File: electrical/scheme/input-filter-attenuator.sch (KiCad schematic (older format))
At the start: 18 parts

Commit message: a.
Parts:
- removed C? (x2): 100n, symbol C
- removed R? (x2): 16 5%, symbol R
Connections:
- wire segments 47 -> 37
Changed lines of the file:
@@
 LIBS:adg5204
 LIBS:ad8620
+LIBS:ad5543
+LIBS:bat54s
 LIBS:digitizer-cache
 EELAYER 25 0
@@
 $Descr A4 11693 8268
 encoding utf-8
-Sheet 2 2
+Sheet 5 7
 Title ""
 Date ""
@@
 U 1 1 55A8C542
 P 5250 3850
+AR Path="/55A8BFF5/55A8C542" Ref="U?"  Part="1"
+AR Path="/55AAF91E/55A8C542" Ref="U?"  Part="1"
+AR Path="/55AAFE8D/55A8C542" Ref="U?"  Part="1"
+AR Path="/55AAFE9C/55A8C542" Ref="U?"  Part="1"
 F 0 "U?" H 5600 3650 60  0000 C CNN
 F 1 "AD8620" H 5600 4050 60  0000 C CNN
@@
 U 2 1 55A8C549
 P 8350 4050
+AR Path="/55A8BFF5/55A8C549" Ref="U?"  Part="2"
+AR Path="/55AAF91E/55A8C549" Ref="U?"  Part="2"
+AR Path="/55AAFE8D/55A8C549" Ref="U?"  Part="2"
+AR Path="/55AAFE9C/55A8C549" Ref="U?"  Part="2"
 F 0 "U?" H 8700 3850 60  0000 C CNN
 F 1 "AD8620" H 8700 4250 60  0000 C CNN
@@
 U 1 1 55A8C74B
 P 5250 2800
+AR Path="/55A8BFF5/55A8C74B" Ref="R?"  Part="1"
+AR Path="/55AAF91E/55A8C74B" Ref="R?"  Part="1"
+AR Path="/55AAFE8D/55A8C74B" Ref="R?"  Part="1"
+AR Path="/55AAFE9C/55A8C74B" Ref="R?"  Part="1"
 F 0 "R?" V 5330 2800 50  0000 C CNN
 F 1 "16 5%" V 5250 2800 50  0000 C CNN
@@
 U 1 1 55A8C77D
 P 5000 3050
+AR Path="/55A8BFF5/55A8C77D" Ref="C?"  Part="1"
+AR Path="/55AAF91E/55A8C77D" Ref="C?"  Part="1"
+AR Path="/55AAFE8D/55A8C77D" Ref="C?"  Part="1"
+AR Path="/55AAFE9C/55A8C77D" Ref="C?"  Part="1"
 F 0 "C?" H 5025 3150 50  0000 L CNN
 F 1 "100n" H 5025 2950 50  0000 L CNN
@@
 U 1 1 55A8C85F
 P 4650 3150
+AR Path="/55A8BFF5/55A8C85F" Ref="#PWR?"  Part="1"
+AR Path="/55AAF91E/55A8C85F" Ref="#PWR?"  Part="1"
+AR Path="/55AAFE8D/55A8C85F" Ref="#PWR?"  Part="1"
+AR Path="/55AAFE9C/55A8C85F" Ref="#PWR?"  Part="1"
 F 0 "#PWR?" H 4650 2900 50  0001 C CNN
 F 1 "GNDA" H 4650 3000 50  0000 C CNN
@@
 U 1 1 55A8C8A7
 P 5250 4800
+AR Path="/55A8BFF5/55A8C8A7" Ref="R?"  Part="1"
+AR Path="/55AAF91E/55A8C8A7" Ref="R?"  Part="1"
+AR Path="/55AAFE8D/55A8C8A7" Ref="R?"  Part="1"
+AR Path="/55AAFE9C/55A8C8A7" Ref="R?"  Part="1"
 F 0 "R?" V 5330 4800 50  0000 C CNN
 F 1 "16 5%" V 5250 4800 50  0000 C CNN
@@
 U 1 1 55A8CC9D
 P 5000 4550
+AR Path="/55A8BFF5/55A8CC9D" Ref="C?"  Part="1"
+AR Path="/55AAF91E/55A8CC9D" Ref="C?"  Part="1"
+AR Path="/55AAFE8D/55A8CC9D" Ref="C?"  Part="1"
+AR Path="/55AAFE9C/55A8CC9D" Ref="C?"  Part="1"
 F 0 "C?" H 5025 4650 50  0000 L CNN
 F 1 "100n" H 5025 4450 50  0000 L CNN
@@
 U 1 1 55A8CCA5
 P 4650 4650
+AR Path="/55A8BFF5/55A8CCA5" Ref="#PWR?"  Part="1"
+AR Path="/55AAF91E/55A8CCA5" Ref="#PWR?"  Part="1"
+AR Path="/55AAFE8D/55A8CCA5" Ref="#PWR?"  Part="1"
+AR Path="/55AAFE9C/55A8CCA5" Ref="#PWR?"  Part="1"
 F 0 "#PWR?" H 4650 4400 50  0001 C CNN
 F 1 "GNDA" H 4650 4500 50  0000 C CNN
@@
 $Comp
 L R R?
-U 1 1 55A8CE4E
-P 8350 3000
-F 0 "R?" V 8430 3000 50  0000 C CNN
-F 1 "16 5%" V 8350 3000 50  0000 C CNN
-F 2 "" V 8280 3000 30  0000 C CNN
-F 3 "" H 8350 3000 30  0000 C CNN
-	1    8350 3000
-	1    0    0    -1
-$EndComp
-$Comp
-L C C?
-U 1 1 55A8CE54
-P 8100 3250
-F 0 "C?" H 8125 3350 50  0000 L CNN
-F 1 "100n" H 8125 3150 50  0000 L CNN
-F 2 "" H 8138 3100 30  0000 C CNN
-F 3 "" H 8100 3250 60  0000 C CNN
-	1    8100 3250
-	0    1    1    0
-$EndComp
-Wire Wire Line
-	8350 3150 8350 3650
-Wire Wire Line
-	8250 3250 8350 3250
-Connection ~ 8350 3250
-Wire Wire Line
-	7950 3250 7750 3250
-Wire Wire Line
-	7750 3250 7750 3350
-$Comp
-L GNDA #PWR?
-U 1 1 55A8CE5F
-P 7750 3350
-F 0 "#PWR?" H 7750 3100 50  0001 C CNN
-F 1 "GNDA" H 7750 3200 50  0000 C CNN
-F 2 "" H 7750 3350 60  0000 C CNN
-F 3 "" H 7750 3350 60  0000 C CNN
-	1    7750 3350
-	1    0    0    -1
-$EndComp
-Wire Wire Line
-	8350 2850 8350 2500
-Text Label 8350 2650 1    60   ~ 0
-v+
-Wire Wire Line
-	8350 4450 8350 4850
-$Comp
-L R R?
-U 1 1 55A8CEC6
-P 8350 5000
-F 0 "R?" V 8430 5000 50  0000 C CNN
-F 1 "16 5%" V 8350 5000 50  0000 C CNN
-F 2 "" V 8280 5000 30  0000 C CNN
-F 3 "" H 8350 5000 30  0000 C CNN
-	1    8350 5000
-	1    0    0    -1
-$EndComp
-Wire Wire Line
-	8350 5150 8350 5450
-Text Label 8350 5400 1    60   ~ 0
-v-
-$Comp
-L C C?
-U 1 1 55A8CECE
-P 8100 4750
-F 0 "C?" H 8125 4850 50  0000 L CNN
-F 1 "100n" H 8125 4650 50  0000 L CNN
-F 2 "" H 8138 4600 30  0000 C CNN
-F 3 "" H 8100 4750 60  0000 C CNN
-	1    8100 4750
-	0    1    1    0
-$EndComp
-Wire Wire Line
-	7950 4750 7750 4750
-Wire Wire Line
-	7750 4750 7750 4850
-$Comp
-L GNDA #PWR?
-U 1 1 55A8CED6
-P 7750 4850
-F 0 "#PWR?" H 7750 4600 50  0001 C CNN
-F 1 "GNDA" H 7750 4700 50  0000 C CNN
-F 2 "" H 7750 4850 60  0000 C CNN
-F 3 "" H 7750 4850 60  0000 C CNN
-	1    7750 4850
-	1    0    0    -1
-$EndComp
-Wire Wire Line
-	8250 4750 8350 4750
-Connection ~ 8350 4750
-$Comp
-L R R?
 U 1 1 55A8D6B2
 P 3100 3650
+AR Path="/55A8BFF5/55A8D6B2" Ref="R?"  Part="1"
+AR Path="/55AAF91E/55A8D6B2" Ref="R?"  Part="1"
+AR Path="/55AAFE8D/55A8D6B2" Ref="R?"  Part="1"
+AR Path="/55AAFE9C/55A8D6B2" Ref="R?"  Part="1"
 F 0 "R?" V 3180 3650 50  0000 C CNN
 F 1 "806 1%" V 3100 3650 50  0000 C CNN
@@
 U 1 1 55A8D707
 P 3600 3650
+AR Path="/55A8BFF5/55A8D707" Ref="R?"  Part="1"
+AR Path="/55AAF91E/55A8D707" Ref="R?"  Part="1"
+AR Path="/55AAFE8D/55A8D707" Ref="R?"  Part="1"
+AR Path="/55AAFE9C/55A8D707" Ref="R?"  Part="1"
 F 0 "R?" V 3680 3650 50  0000 C CNN
 F 1 "1k91 1%" V 3600 3650 50  0000 C CNN
@@
 U 1 1 55A8D733
 P 3850 3900
+AR Path="/55A8BFF5/55A8D733" Ref="C?"  Part="1"
+AR Path="/55AAF91E/55A8D733" Ref="C?"  Part="1"
+AR Path="/55AAFE8D/55A8D733" Ref="C?"  Part="1"
+AR Path="/55AAFE9C/55A8D733" Ref="C?"  Part="1"
 F 0 "C?" H 3875 4000 50  0000 L CNN
 F 1 "22n" H 3875 3800 50  0000 L CNN
@@
 U 1 1 55A8D76D
 P 3350 3350
+AR Path="/55A8BFF5/55A8D76D" Ref="C?"  Part="1"
+AR Path="/55AAF91E/55A8D76D" Ref="C?"  Part="1"
+AR Path="/55AAFE8D/55A8D76D" Ref="C?"  Part="1"
+AR Path="/55AAFE9C/55A8D76D" Ref="C?"  Part="1"
 F 0 "C?" H 3375 3450 50  0000 L CNN
 F 1 "3u3" H 3375 3250 50  0000 L CNN
@@
 U 1 1 55A8D8D4
 P 6200 3850
+AR Path="/55A8BFF5/55A8D8D4" Ref="R?"  Part="1"
+AR Path="/55AAF91E/55A8D8D4" Ref="R?"  Part="1"
+AR Path="/55AAFE8D/55A8D8D4" Ref="R?"  Part="1"
+AR Path="/55AAFE9C/55A8D8D4" Ref="R?"  Part="1"
 F 0 "R?" V 6280 3850 50  0000 C CNN
 F 1 "9k31 1%" V 6200 3850 50  0000 C CNN
@@
 U 1 1 55A8DA7D
 P 6700 3850
+AR Path="/55A8BFF5/55A8DA7D" Ref="R?"  Part="1"
+AR Path="/55AAF91E/55A8DA7D" Ref="R?"  Part="1"
+AR Path="/55AAFE8D/55A8DA7D" Ref="R?"  Part="1"
+AR Path="/55AAFE9C/55A8DA7D" Ref="R?"  Part="1"
 F 0 "R?" V 6780 3850 50  0000 C CNN
 F 1 "21k 1%" V 6700 3850 50  0000 C CNN
@@
 U 1 1 55A8DD2D
 P 6450 3600
+AR Path="/55A8BFF5/55A8DD2D" Ref="C?"  Part="1"
+AR Path="/55AAF91E/55A8DD2D" Ref="C?"  Part="1"
+AR Path="/55AAFE8D/55A8DD2D" Ref="C?"  Part="1"
+AR Path="/55AAFE9C/55A8DD2D" Ref="C?"  Part="1"
 F 0 "C?" H 6475 3700 50  0000 L CNN
 F 1 "120n" H 6475 3500 50  0000 L CNN
@@
 U 1 1 55A8DF47
 P 7050 4200
+AR Path="/55A8BFF5/55A8DF47" Ref="C?"  Part="1"
+AR Path="/55AAF91E/55A8DF47" Ref="C?"  Part="1"
+AR Path="/55AAFE8D/55A8DF47" Ref="C?"  Part="1"
+AR Path="/55AAFE9C/55A8DF47" Ref="C?"  Part="1"
 F 0 "C?" H 7075 4300 50  0000 L CNN
 F 1 "22u" H 7075 4100 50  0000 L CNN
@@
 Wire Wire Line
 	8900 4050 9700 4050
-Wire Wire Line
-	9100 1950 9100 5750
-Wire Wire Line
-	9100 1950 6450 1950
-Wire Wire Line
-	6450 1950 6450 3450
 Connection ~ 9100 4050
 $Comp
@@
 U 1 1 55A8F5C0
 P 7050 4550
+AR Path="/55A8BFF5/55A8F5C0" Ref="#PWR?"  Part="1"
+AR Path="/55AAF91E/55A8F5C0" Ref="#PWR?"  Part="1"
+AR Path="/55AAFE8D/55A8F5C0" Ref="#PWR?"  Part="1"
+AR Path="/55AAFE9C/55A8F5C0" Ref="#PWR?"  Part="1"
 F 0 "#PWR?" H 7050 4300 50  0001 C CNN
 F 1 "GNDA" H 7050 4400 50  0000 C CNN
@@
 U 1 1 55A8F5EF
 P 3850 4250
+AR Path="/55A8BFF5/55A8F5EF" Ref="#PWR?"  Part="1"
+AR Path="/55AAF91E/55A8F5EF" Ref="#PWR?"  Part="1"
+AR Path="/55AAFE8D/55A8F5EF" Ref="#PWR?"  Part="1"
+AR Path="/55AAFE9C/55A8F5EF" Ref="#PWR?"  Part="1"
 F 0 "#PWR?" H 3850 4000 50  0001 C CNN
 F 1 "GNDA" H 3850 4100 50  0000 C CNN
@@
 	4300 5450 5900 5450
 Wire Wire Line
-	7900 4250 7400 4250
-Wire Wire Line
-	7400 4250 7400 5750
-Wire Wire Line
-	7400 5750 9100 5750
+	9100 3300 9100 4700
+Wire Wire Line
+	9100 3300 6450 3300
+Wire Wire Line
+	6450 3300 6450 3450
+Wire Wire Line
+	9100 4700 7700 4700
+Wire Wire Line
+	7700 4700 7700 4250
+Wire Wire Line
+	7700 4250 7900 4250
 $EndSCHEMATC

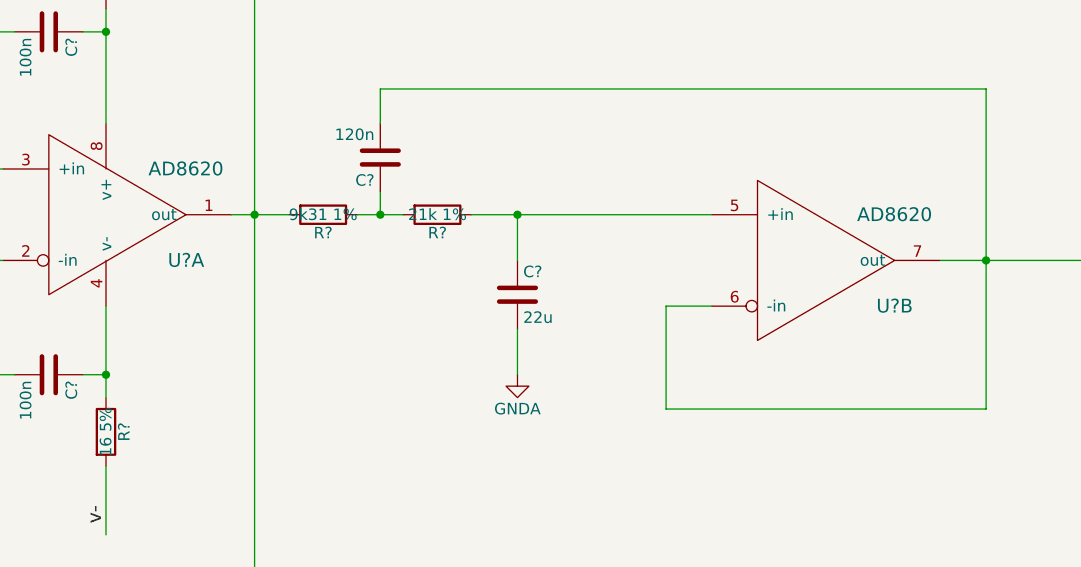
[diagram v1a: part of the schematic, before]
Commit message: Annotated opamps.
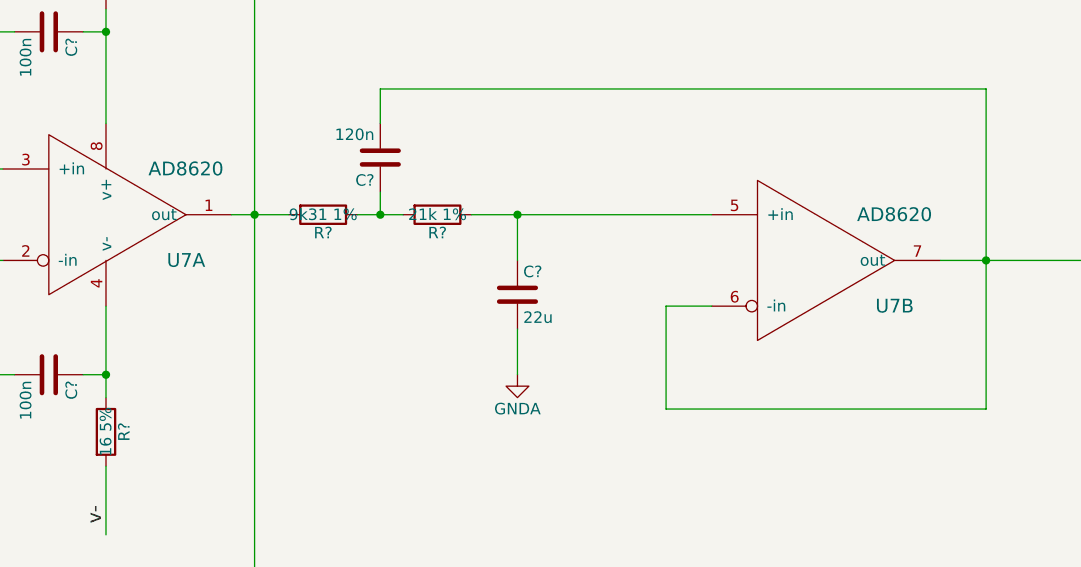
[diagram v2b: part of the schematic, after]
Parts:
- gave numbers to parts that had none: 1
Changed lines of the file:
@@
 $EndDescr
 $Comp
-L AD8620 U?
+L AD8620 U4
 U 1 1 55A8C542
 P 5250 3850
-AR Path="/55A8BFF5/55A8C542" Ref="U?"  Part="1"
-AR Path="/55AAF91E/55A8C542" Ref="U?"  Part="1"
-AR Path="/55AAFE8D/55A8C542" Ref="U?"  Part="1"
-AR Path="/55AAFE9C/55A8C542" Ref="U?"  Part="1"
-F 0 "U?" H 5600 3650 60  0000 C CNN
+AR Path="/55A8BFF5/55A8C542" Ref="U4"  Part="1"
+AR Path="/55AAF91E/55A8C542" Ref="U5"  Part="1"
+AR Path="/55AAFE8D/55A8C542" Ref="U6"  Part="1"
+AR Path="/55AAFE9C/55A8C542" Ref="U7"  Part="1"
+F 0 "U7" H 5600 3650 60  0000 C CNN
 F 1 "AD8620" H 5600 4050 60  0000 C CNN
 F 2 "" H 5300 3850 60  0000 C CNN
@@
 $EndComp
 $Comp
-L AD8620 U?
+L AD8620 U4
 U 2 1 55A8C549
 P 8350 4050
-AR Path="/55A8BFF5/55A8C549" Ref="U?"  Part="2"
-AR Path="/55AAF91E/55A8C549" Ref="U?"  Part="2"
-AR Path="/55AAFE8D/55A8C549" Ref="U?"  Part="2"
-AR Path="/55AAFE9C/55A8C549" Ref="U?"  Part="2"
-F 0 "U?" H 8700 3850 60  0000 C CNN
+AR Path="/55A8BFF5/55A8C549" Ref="U4"  Part="2"
+AR Path="/55AAF91E/55A8C549" Ref="U5"  Part="2"
+AR Path="/55AAFE8D/55A8C549" Ref="U6"  Part="2"
+AR Path="/55AAFE9C/55A8C549" Ref="U7"  Part="2"
+F 0 "U7" H 8700 3850 60  0000 C CNN
 F 1 "AD8620" H 8700 4250 60  0000 C CNN
 F 2 "" H 8400 4050 60  0000 C CNN

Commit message: a
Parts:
- C40, C41, C42, C43, C44: renamed from C?; footprint (none) -> Capacitors_SMD:C_0805_HandSoldering
- C45: renamed from C?; value 22u -> 22n; footprint (none) -> Capacitors_SMD:C_0805_HandSoldering
- R43, R44, R45, R46, R47, R48: renamed from R?; footprint (none) -> Resistors_SMD:R_0805_HandSoldering
- U4: value AD8620 -> AD8672; footprint (none) -> Housings_SOIC:SOIC-8_3.9x4.9mm_Pitch1.27mm
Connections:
- wire segments 37 -> 39
